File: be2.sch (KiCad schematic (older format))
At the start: 34 parts, among them K1 mini_banana_jack, K2 mini_banana_jack, K3 mini_banana_jack, K4 mini_banana_jack, K5 mini_banana_jack, K6 mini_banana_jack, U1 AD620A, U2 TL082

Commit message: modifs
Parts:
- removed R6, R7: 220k, Resistors_SMD:R_0805, symbol R_Small
- added C10: 10n, Capacitors_SMD:C_0805, symbol C_Small
- added unit 2 of U2
- added unit 2 of U3
- C5, C9: value 220n -> 330n; footprint Capacitors_SMD:C_0805 -> Capacitors_ThroughHole:C_Disc_D3_P2.5
- C8: value 220n -> 10n
- R1: value 100K -> 270k
- R4, R5: value 220k -> 100K
- R8, R9: value 1k -> 10K
- renumbered U2 to U3
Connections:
- net labels added: neg_out_buff
- wire segments 79 -> 96
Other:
- note added: "+PSPICE \n\n* discrete\n.include ./sim/lib/1N4148.mdl\n* ic\n.include ./sim/lib/AD620A.ckt\n.include ./sim/lib/TL082.ckt\n* misc\n.include ./sim/lib/jumper.ckt\n\n* power\nv1 vcc 0 15v\nv2 vss 0 -15v\n\n* input\nv3 /in+ gnd sine 0 10 1k 0 0 90 DC 0 AC 1\nv4 /in- gnd DC 0 \n\n* transient sim, 1ms->1s, no op init\n.tran 0 1s 1m uic\n\n* ac sim\n*.ac dec 1K 1 1Meg\n\n*step\n*.step param R 1K 100K 10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"
- note removed: "+PSPICE \n\n* discrete\n.include ./sim/lib/1N4148.mdl\n* ic\n.include ./sim/lib/AD620A.ckt\n.include ./sim/lib/TL082.ckt\n* misc\n.include ./sim/lib/jumper.ckt\n\n* power\nv1 vcc 0 15v\nv2 vss 0 -15v\n\n* input\nv3 /in+ gnd sine 0 2 1k 0 0 90 DC 0 AC 1\nv4 /in- gnd sine 0 -100m 1k 0 0 90 DC 0 \n\n* transient sim, 1ms->1s, no op init\n.tran 0 1s 1m uic\n\n* ac sim\n*.ac dec 1K 1 1Meg\n \n\n"
- moved on the sheet: D5, D6

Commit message: forgot feedback :<
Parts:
- JP2: value jp_close -> jp_open
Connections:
- wire segments 96 -> 97
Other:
- note added: "+PSPICE \n\n* discrete\n.include ./sim/lib/1N4148.mdl\n* ic\n.include ./sim/lib/AD620A.ckt\n.include ./sim/lib/TL082.ckt\n* misc\n.include ./sim/lib/jumper.ckt\n\n* power\nv1 vcc 0 15v\nv2 vss 0 -15v\n\n* input\nv4 /in- gnd DC 0 \n*v3 /in+ gnd sine 0 10 1k 0 0 90 DC 0 AC 1\nv3 /mean_in gnd sine 0 10 1k 0 0 90 DC 0 AC 1\n\n* transient sim, 1ms->1s, no op init\n*.tran 0 1s 1m uic\n\n* ac sim\n.ac d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"
- note removed: "+PSPICE \n\n* discrete\n.include ./sim/lib/1N4148.mdl\n* ic\n.include ./sim/lib/AD620A.ckt\n.include ./sim/lib/TL082.ckt\n* misc\n.include ./sim/lib/jumper.ckt\n\n* power\nv1 vcc 0 15v\nv2 vss 0 -15v\n\n* input\nv3 /in+ gnd sine 0 10 1k 0 0 90 DC 0 AC 1\nv4 /in- gnd DC 0 \n\n* transient sim, 1ms->1s, no op init\n.tran 0 1s 1m uic\n\n* ac sim\n*.ac dec 1K 1 1Meg\n\n*step\n*.step param R 1K 100K 10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"
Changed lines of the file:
@@
 neg_in
 Text Notes 650  7950 0    60   ~ 12
-+PSPICE  \n\n* discrete\n.include ./sim/lib/1N4148.mdl\n* ic\n.include ./sim/lib/AD620A.ckt\n.include ./sim/lib/TL082.ckt\n* misc\n.include ./sim/lib/jumper.ckt\n\n* power\nv1 vcc 0 15v\nv2 vss 0 -15v\n\n* input\nv3 /in+ gnd sine 0 10 1k 0 0 90 DC 0 AC 1\nv4 /in-  gnd  DC 0 \n\n* transient sim, 1ms->1s, no op init\n.tran 0 1s 1m uic\n\n* ac  sim\n*.ac dec 1K 1 1Meg\n\n*step\n*.step param R 1K 100K 10K\n\n\n \n\n
++PSPICE  \n\n* discrete\n.include ./sim/lib/1N4148.mdl\n* ic\n.include ./sim/lib/AD620A.ckt\n.include ./sim/lib/TL082.ckt\n* misc\n.include ./sim/lib/jumper.ckt\n\n* power\nv1 vcc 0 15v\nv2 vss 0 -15v\n\n* input\nv4 /in-  gnd  DC 0 \n*v3 /in+ gnd sine 0 10 1k 0 0 90 DC 0 AC 1\nv3 /mean_in gnd sine 0 10 1k 0 0 90 DC 0 AC 1\n\n* transient sim, 1ms->1s, no op init\n*.tran 0 1s 1m uic\n\n* ac  sim\n.ac dec 1K 1 1Meg\n\n*step\n*.step param R 1K 100K 10K\n\n\n \n\n
 Wire Wire Line
 	1400 1650 2200 1650
@@
 	14150 2950 14600 2950
 Wire Wire Line
-	14600 2950 14600 3650
+	14600 2950 14600 4300
 Wire Wire Line
 	14400 3650 14900 3650
@@
 	1    0    0    -1
 $EndComp
-$Comp
-L GND #PWR024
-U 1 1 56E36E6A
-P 13750 4200
-F 0 "#PWR024" H 13750 3950 50  0001 C CNN
-F 1 "GND" H 13758 4026 50  0000 C CNN
-F 2 "" H 13750 4200 50  0000 C CNN
-F 3 "" H 13750 4200 50  0000 C CNN
-	1    13750 4200
-	1    0    0    -1
-$EndComp
-Wire Wire Line
-	13750 4200 13750 3750
+Wire Wire Line
+	13750 3750 13750 4300
 Wire Wire Line
 	13750 3750 13800 3750
@@
 P 11750 4000
 F 0 "JP2" V 11669 3856 50  0000 R CNN
-F 1 "jp_close" V 11600 3850 50  0000 R CNN
+F 1 "jp_open" V 11600 3850 50  0000 R CNN
 F 2 "Pin_Headers:Pin_Header_Straight_2x01" H 11750 4000 50  0001 C CNN
 F 3 "" H 11750 4000 50  0000 C CNN
@@
 mean_out
 $Comp
-L VCC #PWR025
+L VCC #PWR024
 U 1 1 56E4467E
 P 13600 5200
-F 0 "#PWR025" H 13600 5050 50  0001 C CNN
+F 0 "#PWR024" H 13600 5050 50  0001 C CNN
 F 1 "VCC" V 13621 5327 50  0000 L CNN
 F 2 "" H 13600 5200 50  0000 C CNN
@@
 $EndComp
 $Comp
-L VSS #PWR026
+L VSS #PWR025
 U 1 1 56E44690
 P 14500 5200
-F 0 "#PWR026" H 14500 5050 50  0001 C CNN
+F 0 "#PWR025" H 14500 5050 50  0001 C CNN
 F 1 "VSS" V 14520 5328 50  0000 L CNN
 F 2 "" H 14500 5200 50  0000 C CNN
@@
 $EndComp
 $Comp
-L GND #PWR027
+L GND #PWR026
 U 1 1 56E44696
 P 14050 5400
-F 0 "#PWR027" H 14050 5150 50  0001 C CNN
+F 0 "#PWR026" H 14050 5150 50  0001 C CNN
 F 1 "GND" H 14058 5226 50  0000 C CNN
 F 2 "" H 14050 5400 50  0000 C CNN
@@
 	13700 1650 13750 1650
 $Comp
-L VSS #PWR028
+L VSS #PWR027
 U 1 1 56E497C9
 P 13950 1900
-F 0 "#PWR028" H 13950 1750 50  0001 C CNN
+F 0 "#PWR027" H 13950 1750 50  0001 C CNN
 F 1 "VSS" H 13971 2074 50  0000 C CNN
 F 2 "" H 13950 1900 50  0000 C CNN
@@
 $EndComp
 $Comp
-L VCC #PWR029
+L VCC #PWR028
 U 1 1 56E49BA9
 P 13950 1200
-F 0 "#PWR029" H 13950 1050 50  0001 C CNN
+F 0 "#PWR028" H 13950 1050 50  0001 C CNN
 F 1 "VCC" H 13970 1374 50  0000 C CNN
 F 2 "" H 13950 1200 50  0000 C CNN
@@
 	14500 1550 14350 1550
 $Comp
-L GND #PWR030
+L GND #PWR029
 U 1 1 56E4EDE4
 P 13650 1450
-F 0 "#PWR030" H 13650 1200 50  0001 C CNN
+F 0 "#PWR029" H 13650 1200 50  0001 C CNN
 F 1 "GND" V 13658 1322 50  0000 R CNN
 F 2 "" H 13650 1450 50  0000 C CNN
@@
 Wire Wire Line
 	13750 1450 13650 1450
+Wire Wire Line
+	13750 4300 14600 4300
 $EndSCHEMATC

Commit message: we're routed, fall back!
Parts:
- removed C1, C2: 10u, Capacitors_ThroughHole:C_Radial_D5_L6_P2.5, symbol CP_Small
- removed K1, K2, K3, K4, K5, K6: mini_banana_jack, lib:mini_banana_jack_2mm, symbol mini_banana_jack
- added C1, C2: 1u, Capacitors_SMD:C_1206, symbol C_Small
- added K1: CONN_01X03, lib:Pin_Header_Straight_1x03_phelma, symbol CONN_01X03
- added K2: CONN_01X02, lib:Pin_Header_Straight_1x02_phelma, symbol CONN_01X02
- added K3: CONN_01X01, lib:Pin_Header_Straight_1x01_phelma, symbol CONN_01X01
- C10, C3, C4, C6, C7, C8: footprint Capacitors_SMD:C_0805 -> Capacitors_SMD:C_1206
- C5, C9: footprint Capacitors_ThroughHole:C_Disc_D3_P2.5 -> Capacitors_SMD:C_1206
- D1, D2, D3, D4, D5, D6: footprint Diodes_ThroughHole:Diode_DO-35_SOD27_Horizontal_RM10 -> lib:Diode_DO-41_SOD81_Vertical_AnodeUp_phelma
- JP1: footprint Pin_Headers:Pin_Header_Straight_2x01 -> lib:JP_20mil
- JP2: value jp_open -> jp_close; footprint Pin_Headers:Pin_Header_Straight_2x01 -> lib:JP_20mil
- R1, R2, R3, R4, R5, R8, R9: footprint Resistors_SMD:R_0805 -> Resistors_SMD:R_1206
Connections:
- wire segments 97 -> 106
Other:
- note added: "+PSPICE \n\n* discrete\n.include ./sim/lib/1N4148.mdl\n* ic\n.include ./sim/lib/AD620A.ckt\n.include ./sim/lib/TL082.ckt\n* misc\n.include ./sim/lib/jumper.ckt\n\n* power\nv1 vcc 0 15v\nv2 vss 0 -15v\n\n* input\nv4 /in- gnd DC 0 \nv3 /in+ gnd sine 0 10 1k 0 0 90 DC 0 AC 1\n*v3 /mean_in gnd sine 0 10 1k 0 0 90 DC 0 AC 1\n\n* transient sim, 1ms->1s, no op init\n.tran 0 10s 1m uic\n\n* ac sim\n*.ac 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"
- note removed: "+PSPICE \n\n* discrete\n.include ./sim/lib/1N4148.mdl\n* ic\n.include ./sim/lib/AD620A.ckt\n.include ./sim/lib/TL082.ckt\n* misc\n.include ./sim/lib/jumper.ckt\n\n* power\nv1 vcc 0 15v\nv2 vss 0 -15v\n\n* input\nv4 /in- gnd DC 0 \n*v3 /in+ gnd sine 0 10 1k 0 0 90 DC 0 AC 1\nv3 /mean_in gnd sine 0 10 1k 0 0 90 DC 0 AC 1\n\n* transient sim, 1ms->1s, no op init\n*.tran 0 1s 1m uic\n\n* ac sim\n.ac d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"

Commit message: some changes, simu ...
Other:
- note added: "+PSPICE \n\n* discrete\n.include ./sim/lib/1N4148.mdl\n* ic\n.include ./sim/lib/AD620A.ckt\n.include ./sim/lib/TL082.ckt\n* misc\n.include ./sim/lib/jumper.ckt\n\n* power\nv1 vcc 0 15v\nv2 vss 0 -15v\n\n* input\nv4 /in- gnd DC 0 \nv3 /in+ gnd sine 0 10 40k 0 0 90 DC 0 AC 2.62\n*v3 /mean_in gnd sine 0 10 1k 0 0 90 DC 0 AC 1\n\n* transient sim, 1ms->1s, no op init\n.tran 0 10s 1m uic\n\n* ac sim\n*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"
- note removed: "+PSPICE \n\n* discrete\n.include ./sim/lib/1N4148.mdl\n* ic\n.include ./sim/lib/AD620A.ckt\n.include ./sim/lib/TL082.ckt\n* misc\n.include ./sim/lib/jumper.ckt\n\n* power\nv1 vcc 0 15v\nv2 vss 0 -15v\n\n* input\nv4 /in- gnd DC 0 \nv3 /in+ gnd sine 0 10 1k 0 0 90 DC 0 AC 1\n*v3 /mean_in gnd sine 0 10 1k 0 0 90 DC 0 AC 1\n\n* transient sim, 1ms->1s, no op init\n.tran 0 10s 1m uic\n\n* ac sim\n*.ac 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"
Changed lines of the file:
@@
 neg_in
 Text Notes 650  7950 0    60   ~ 12
-+PSPICE  \n\n* discrete\n.include ./sim/lib/1N4148.mdl\n* ic\n.include ./sim/lib/AD620A.ckt\n.include ./sim/lib/TL082.ckt\n* misc\n.include ./sim/lib/jumper.ckt\n\n* power\nv1 vcc 0 15v\nv2 vss 0 -15v\n\n* input\nv4 /in-  gnd  DC 0 \nv3 /in+ gnd sine 0 10 1k 0 0 90 DC 0 AC 1\n*v3 /mean_in gnd sine 0 10 1k 0 0 90 DC 0 AC 1\n\n* transient sim, 1ms->1s, no op init\n.tran 0 10s 1m uic\n\n* ac  sim\n*.ac dec 1K 1 1Meg\n\n*step\n*.step param R 1K 100K 10K\n\n\n \n\n
++PSPICE  \n\n* discrete\n.include ./sim/lib/1N4148.mdl\n* ic\n.include ./sim/lib/AD620A.ckt\n.include ./sim/lib/TL082.ckt\n* misc\n.include ./sim/lib/jumper.ckt\n\n* power\nv1 vcc 0 15v\nv2 vss 0 -15v\n\n* input\nv4 /in-  gnd  DC 0 \nv3 /in+ gnd sine 0 10 40k 0 0 90 DC 0 AC 2.62\n*v3 /mean_in gnd sine 0 10 1k 0 0 90 DC 0 AC 1\n\n* transient sim, 1ms->1s, no op init\n.tran 0 10s 1m uic\n\n* ac  sim\n*.ac dec 1K 1 1Meg\n\n*step\n*.step param R 1K 100K 10K\n\n\n \n\n
 Text Label 7600 4300 3    60   ~ 0
 u2_out

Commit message: ugly merge
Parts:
- added D? (x4): LED, symbol LED
- added K?: CONN_01X03, symbol CONN_01X03
- added K?: CONN_01X01, symbol CONN_01X01
- added R?: 100K, symbol R_Small
- added R?: 1K, symbol R_Small
- added R? (x4): R_Small, symbol R_Small
- added R?: 100, symbol R_Small
- added U? (x2): TL082, symbol TL082
- added U? (x4): LM311N, symbol LM311N
- added jp_close? (x2): JP3, symbol CONN_01X02
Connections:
- net GND: now also K?.1 (P1), R?.2, R?.2
- net VCC: now also K?.3 (P3), R?.1, R?.1, U?.4 (V-), U?.8 (V+), U?.8 (V+), U?.8 (V+), U?.8 (V+), U?.8 (V+)
- net VSS: now also K?.2 (P2), U?.1 (GND), U?.1 (GND), U?.1 (GND), U?.1 (GND), U?.4 (V-), U?.4 (V-), U?.4 (V-), U?.4 (V-), U?.4 (V-), U?.8 (V+)
- new net: R?.1, R?.2, U?.2 (-)
- new net: D?.1 (K), U?.7 (x4)
- new net amp_in: K?.1 (P1), U?.3 (+), jp_close?.1 (P1)
- new net amp_out: R?.1, U?.1, jp_close?.1 (P1)
- new net comp_in_x1: U?.3 (-), U?.3 (-), jp_close?.2 (P2)
- new net comp_in_x100: U?.3 (-), U?.3 (-), jp_close?.2 (P2)
- new net led_current_source: D?.2 (A), D?.2 (A), D?.2 (A), D?.2 (A), R?.2, U?.1, U?.2 (-)
- new net ref_10v_div_pi: R?.1, R?.2, U?.2 (+), U?.2 (+)
- new net ref_1v_div_pi: R?.1, R?.2, U?.2 (+), U?.2 (+)
- new net ref_led: R?.1, R?.2, U?.3 (+)

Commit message: part2 + routing
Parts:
- removed R?: 100, symbol R_Small
- removed R?: R_Small, symbol R_Small
- removed U?: TL082, symbol TL082
- added C11, C12: 10n, Capacitors_SMD:C_1206, symbol C_Small
- added R100, R101, R102, R103: 1k, Resistors_SMD:R_1206, symbol R_Small
- D100, D101, D102, D103: renamed from D?; footprint (none) -> lib:KP-3216SRC-PRV
- K4: renamed from K?; footprint (none) -> lib:Pin_Header_Straight_1x03_phelma
- K5: renamed from K?; footprint (none) -> lib:Pin_Header_Straight_1x01_phelma
- R11, R12, R13, R6, R7: renamed from R?; footprint (none) -> Resistors_SMD:R_1206
- U1: symbol AD620 -> AD620-RESCUE-be2
- U100, U101, U102, U103, U4: renamed from U?; footprint (none) -> Housings_SOIC:SOIC-8_3.9x4.9mm_Pitch1.27mm
- jp_close1, jp_close2: renamed from jp_close?; footprint (none) -> lib:JP_20mil
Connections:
- net mean_out is gone; now on net amp_in: C9.1, K3.1 (P1), U3.1, U3.2 (-), U3.5 (+)
- net ref_led is gone; now on net VCC: R11.1
- net GND: now also C11.1, C12.2
- net VCC: now also C11.2, R100.1, R101.1, R102.1, R103.1
- net VSS: now also C12.1
- removed net led_current_source: D100.2 (A), D101.2 (A), D102.2 (A), D103.2 (A)
- new net: D103.2 (A), R103.2
- new net: D102.2 (A), R102.2
- new net: D101.2 (A), R101.2
- new net: D100.2 (A), R100.2
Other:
- moved on the sheet: D100, D101, D102, D103, R11, R12, R13, R6, R7, U100, U101, U102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

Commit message: datasheet:pinout, cleaned schem
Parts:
- added R?: 220k, Resistors_SMD:R_1206, symbol R_Small
- added R?: 15k, Resistors_SMD:R_1206, symbol R_Small
- R100, R101, R102, R103: value 1k -> 12k
- R11: value R_Small -> 39k
- R12: value R_Small -> 10k
- R13: value R_Small -> 1.2k
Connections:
- net GND: now also R?.1; no longer C11.1, C12.2
- net VCC: now also R?.2
- net ref_10v_div_pi: now also R?.1
- net ref_1v_div_pi: now also R?.2
- new net: C11.1, C12.2
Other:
- note added: "KA-001 module"
- note added: "KA-002 module"
- moved on the sheet: C1, C10, C11, C12, C2, C3, C4, C5, C6, C7, C8, C9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

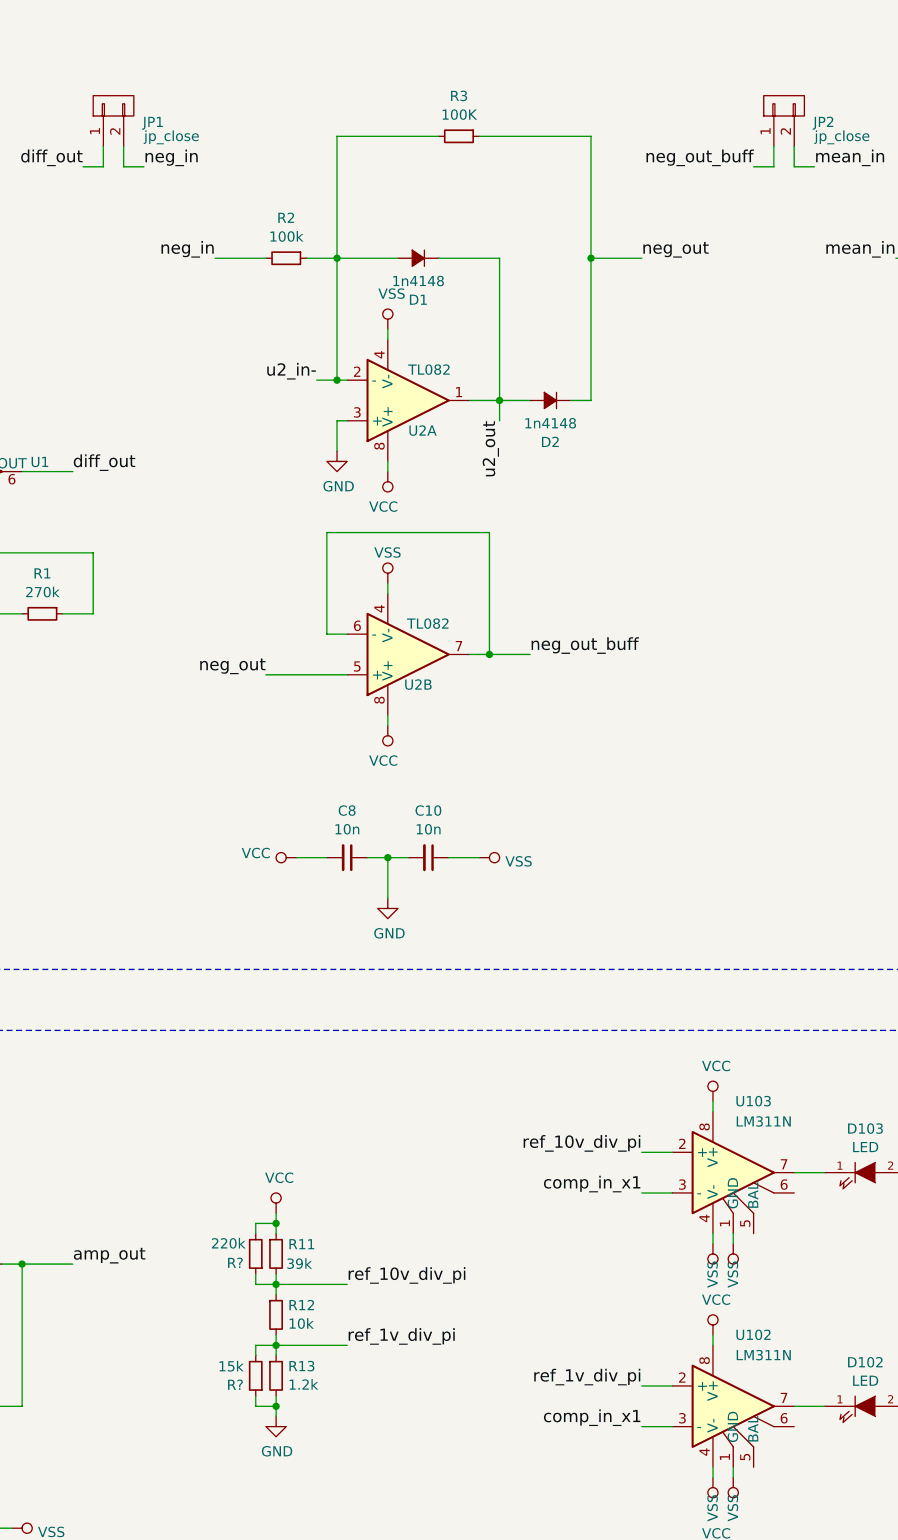
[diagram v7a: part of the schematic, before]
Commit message: datasheet:absolute max ratings, schem+pcb:minor modifs
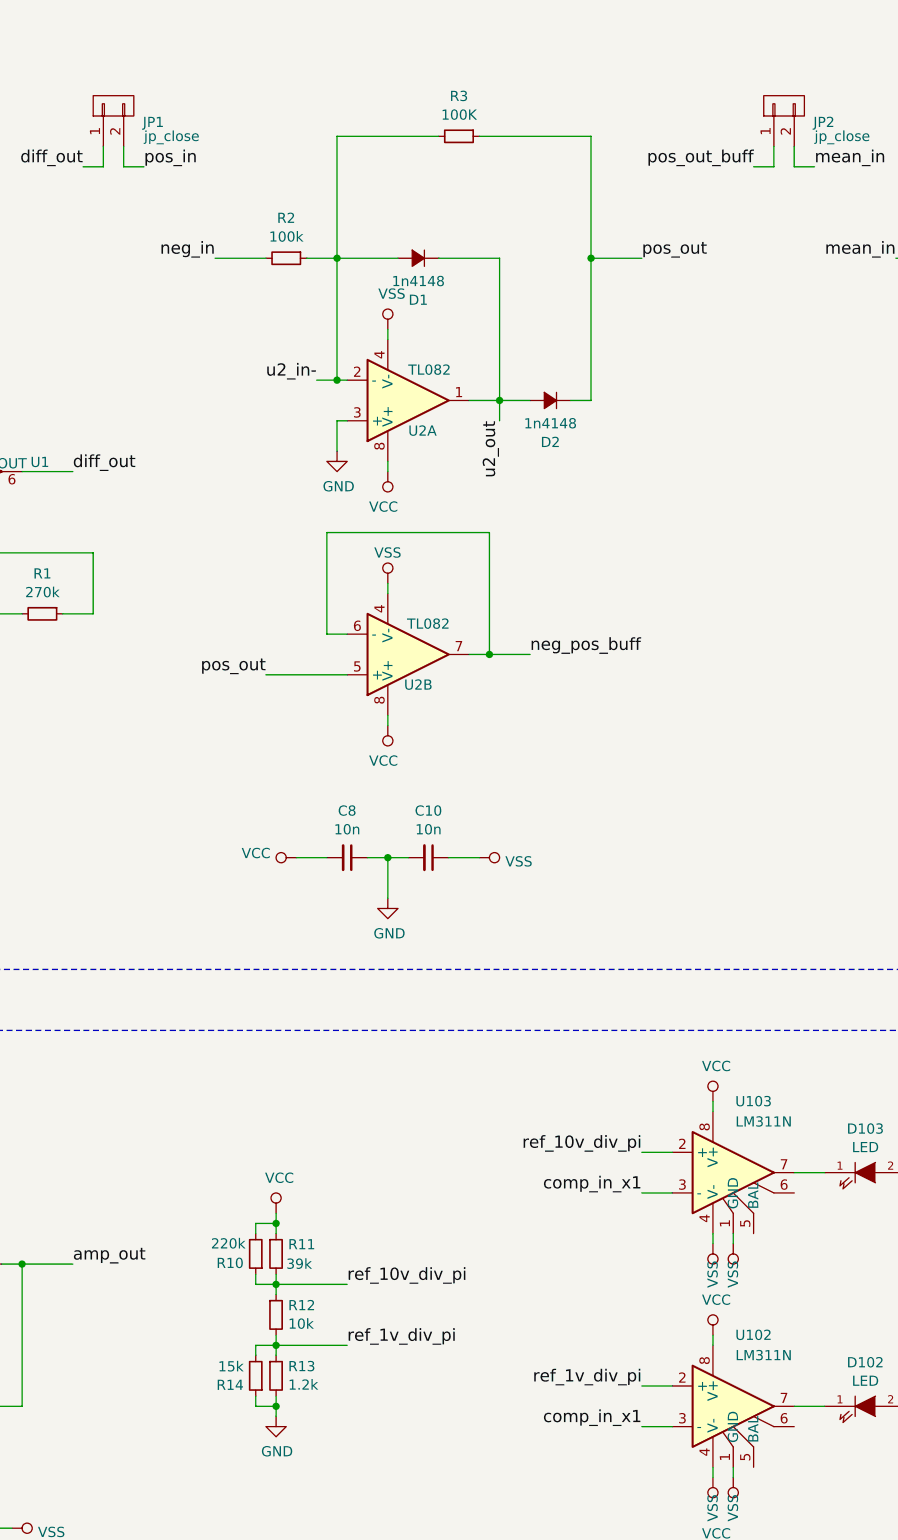
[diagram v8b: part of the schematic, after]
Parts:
- gave numbers to parts that had none: 2
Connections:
- net neg_in: no longer JP1.2 (P2)
- net neg_out renamed pos_out
- net neg_out_buff renamed neg_pos_buff
- net neg_pos_buff: no longer JP2.1 (P1)
- new net pos_in: JP1.2 (P2)
- new net pos_out_buff: JP2.1 (P1)
